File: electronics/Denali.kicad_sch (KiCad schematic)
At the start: 5 parts, among them J1 Conn_01x04, J2 Conn_01x04, J3 Conn_01x04, J4 Conn_01x04, U1 kb2040

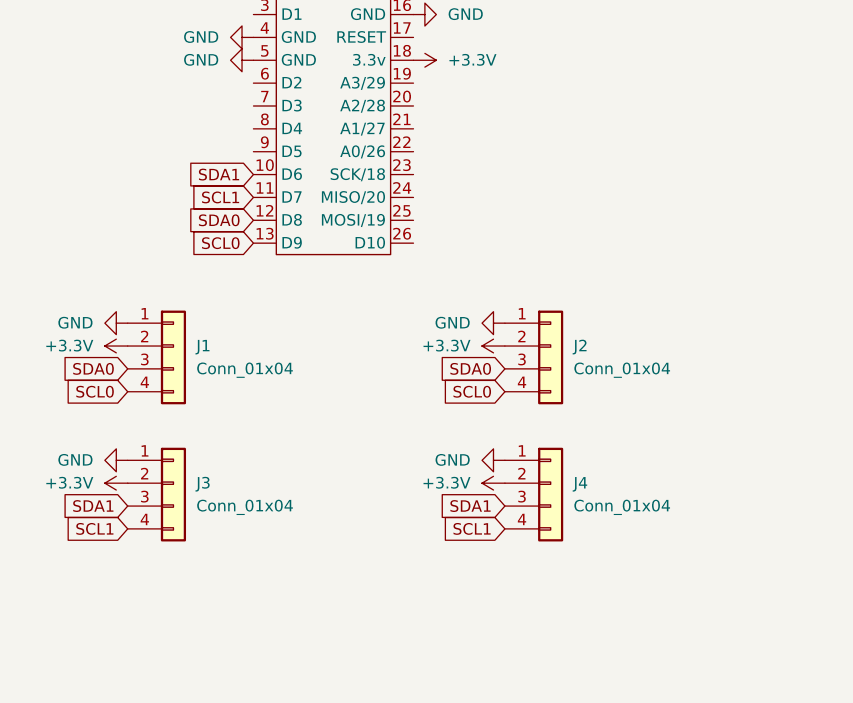
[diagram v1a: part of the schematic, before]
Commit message: begin matrix via diodes
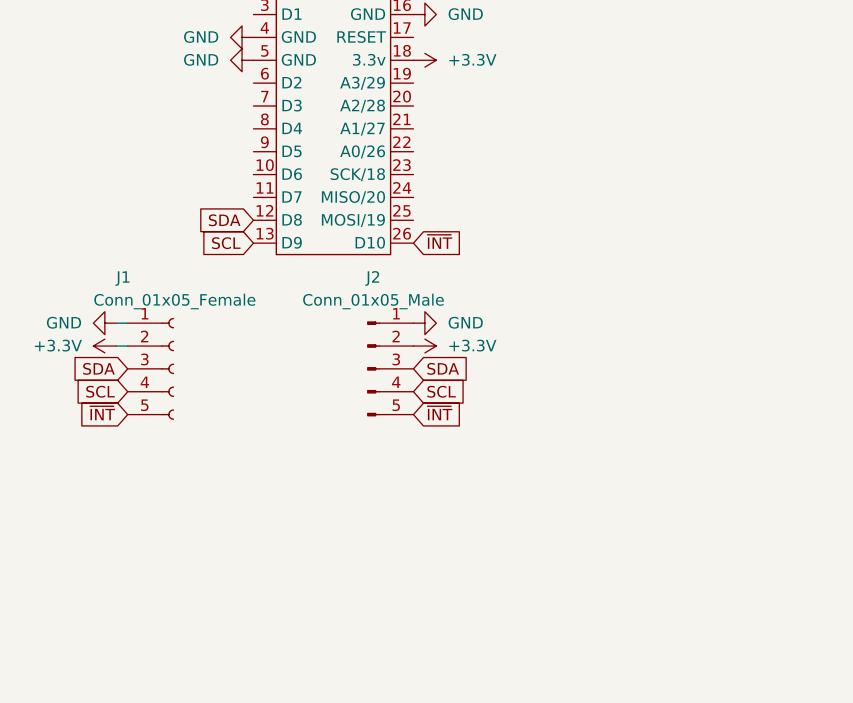
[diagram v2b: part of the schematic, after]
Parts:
- removed J1, J2, J3, J4: Conn_01x04, symbol Connector_Generic:Conn_01x04
- added J1: Conn_01x05_Female, Connector_PinHeader_2.54mm:PinHeader_1x05_P2.54mm_Vertical, symbol Connector:Conn_01x05_Female
- added J2: Conn_01x05_Male, Connector_PinHeader_2.54mm:PinHeader_1x05_P2.54mm_Vertical, symbol Connector:Conn_01x05_Male
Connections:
- net +3V3: now also J1.2 (Pin_2), J2.2 (Pin_2)
- net GND: now also J1.1 (Pin_1), J2.1 (Pin_1)
- net ~{INT}: now reaches U1.26 (D10)
- net ~{INT}: now also J1.5 (Pin_5), J2.5 (Pin_5)
- net SCL0 renamed SCL
- net SCL: now also J1.4 (Pin_4), J2.4 (Pin_4)
- net SCL1: no longer names the net of U1.11 (D7)
- net SDA0 renamed SDA
- net SDA: now also J1.3 (Pin_3), J2.3 (Pin_3)
- net SDA1: no longer names the net of U1.10 (D6)
